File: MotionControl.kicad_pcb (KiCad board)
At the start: 2 copper layers, 180 x 80 mm, 176 parts, among them J1 Screw_Terminal_01x02, J10 Screw_Terminal_01x02, J11 Screw_Terminal_01x02, J2 Conn_ARM_JTAG_SWD_10, J3 Screw_Terminal_01x04, J5 Screw_Terminal_01x04, J6 Screw_Terminal_01x04, J7 Screw_Terminal_01x04, J8 Screw_Terminal_01x02, J9 Screw_Terminal_01x02, P1 USB_C_Plug_USB2.0, Q1 2N7002, Q10 Q_NMOS_DGS, Q11 Q_NMOS_DGS, Q12 Q_NMOS_DGS, Q13 Q_NMOS_DGS, Q14 Q_NMOS_DGS, Q15 Q_NMOS_DGS, Q16 Q_NMOS_DGS, Q17 Q_NMOS_DGS, Q18 Q_NMOS_DGS, Q19 Q_NMOS_DGS, Q2 Q_NMOS_DGS, Q20 Q_NMOS_DGS, Q21 Q_NMOS_DGS, Q22 Q_NMOS_DGS, Q23 Q_NMOS_DGS, Q24 Q_NMOS_DGS, Q25 Q_NMOS_DGS, Q26 Q_NMOS_DGS, Q27 Q_NMOS_DGS, Q28 Q_NMOS_DGS, Q29 Q_NMOS_DGS, Q3 Q_NMOS_DGS, Q30 Q_NMOS_DGS, Q31 Q_NMOS_DGS, Q32 Q_NMOS_DGS, Q33 Q_NMOS_DGS, Q4 Q_NMOS_DGS, Q5 Q_NMOS_DGS, Q6 Q_NMOS_DGS, Q7 Q_NMOS_DGS, Q8 Q_NMOS_DGS, Q9 Q_NMOS_DGS, SW1 SW_Push, U1 ATSAMD21J18A-A, U2 AP2112K-3.3, U3 TMC5160A-TA, U4 TMC5160A-TA, U5 TMC5160A-TA, U6 TMC5160A-TA, U7 TC4427, Y1 32.768kHz

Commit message: Route swd header
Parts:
- moved D6 27.1 mm to (130.0, 95.0), turned to 90 degrees
- moved J2 23.5 mm to (123.7, 86.1), turned to 90 degrees
- moved R9 20.7 mm to (130.0, 92.3), turned to 90 degrees
- moved D5 17.6 mm to (127.7, 95.0), turned to 90 degrees
- moved R8 11.4 mm to (127.7, 92.3), turned to 90 degrees
- moved C7 0.46 mm to (156.3, 81.7)
- moved C11 0.41 mm to (157.4, 81.7)
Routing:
- net /Steppers/MISO: track 0.00 -> 74.7 mm, vias 0 -> 2
- net /Steppers/MOSI: track 0.00 -> 71.1 mm, vias 0 -> 2
- net /Steppers/SCK: track 0.00 -> 67.1 mm, vias 0 -> 2
- net +5V: track 266.2 -> 326.4 mm, vias 1 -> 2
- net SWDCLK: track 0.00 -> 45.5 mm
- net PA27_TX_LED: track 0.00 -> 38.5 mm
- net SWDIO: track 0.00 -> 38.2 mm
- net /RESETn: track 16.0 -> 50.9 mm, vias 0 -> 2
- net +3V3: track 302.7 -> 331.1 mm, vias 0 -> 2
- net PB03_RX_LED: track 0.00 -> 28.1 mm, vias 0 -> 2
- net Net-(D6-A): track 0.00 -> 1.45 mm
- net Net-(D5-A): track 0.00 -> 1.45 mm
- net /Steppers/Stepper Unit/LED_OUT: track 49.5 -> 50.0 mm, vias 0 -> 2
- net GND: vias 74 -> 88
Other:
- board text added: "RX"
- board text added: "SWD"
- board text added: "TX"

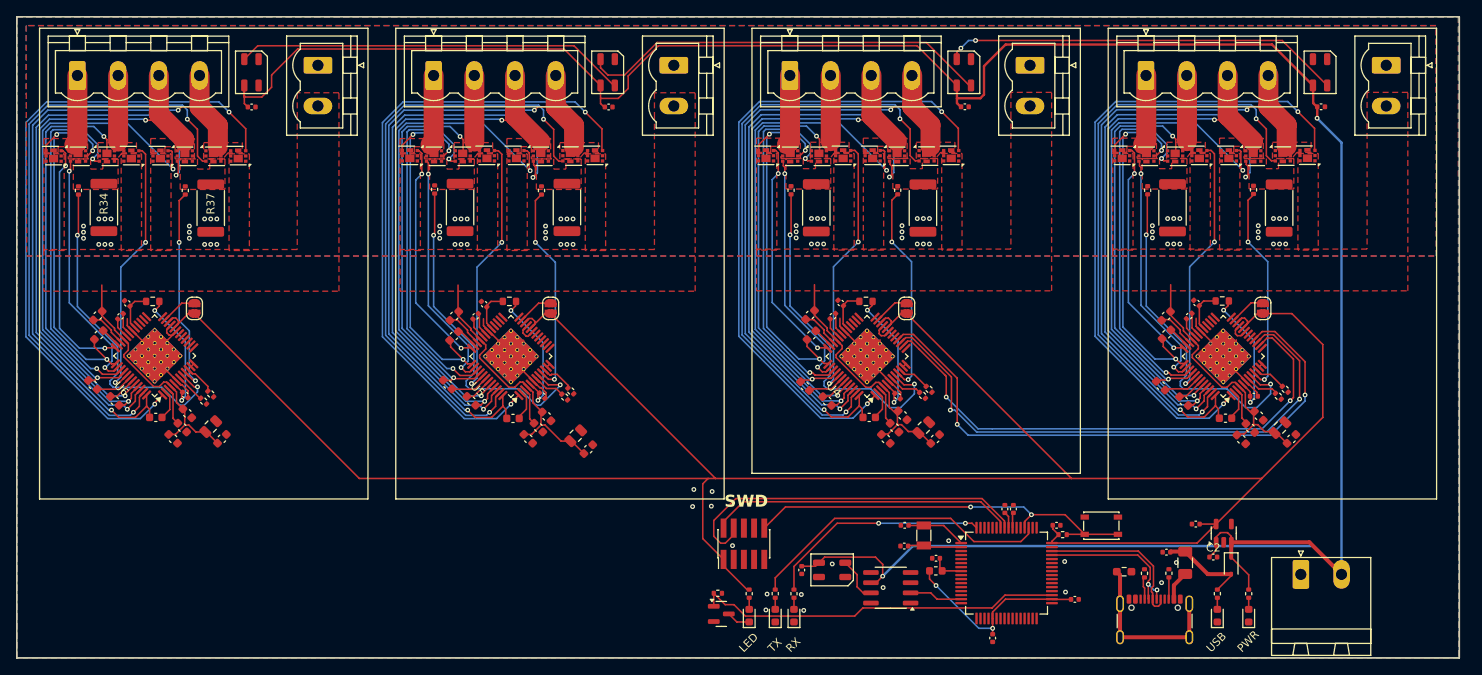
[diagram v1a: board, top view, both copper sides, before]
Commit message: Begin spi routing
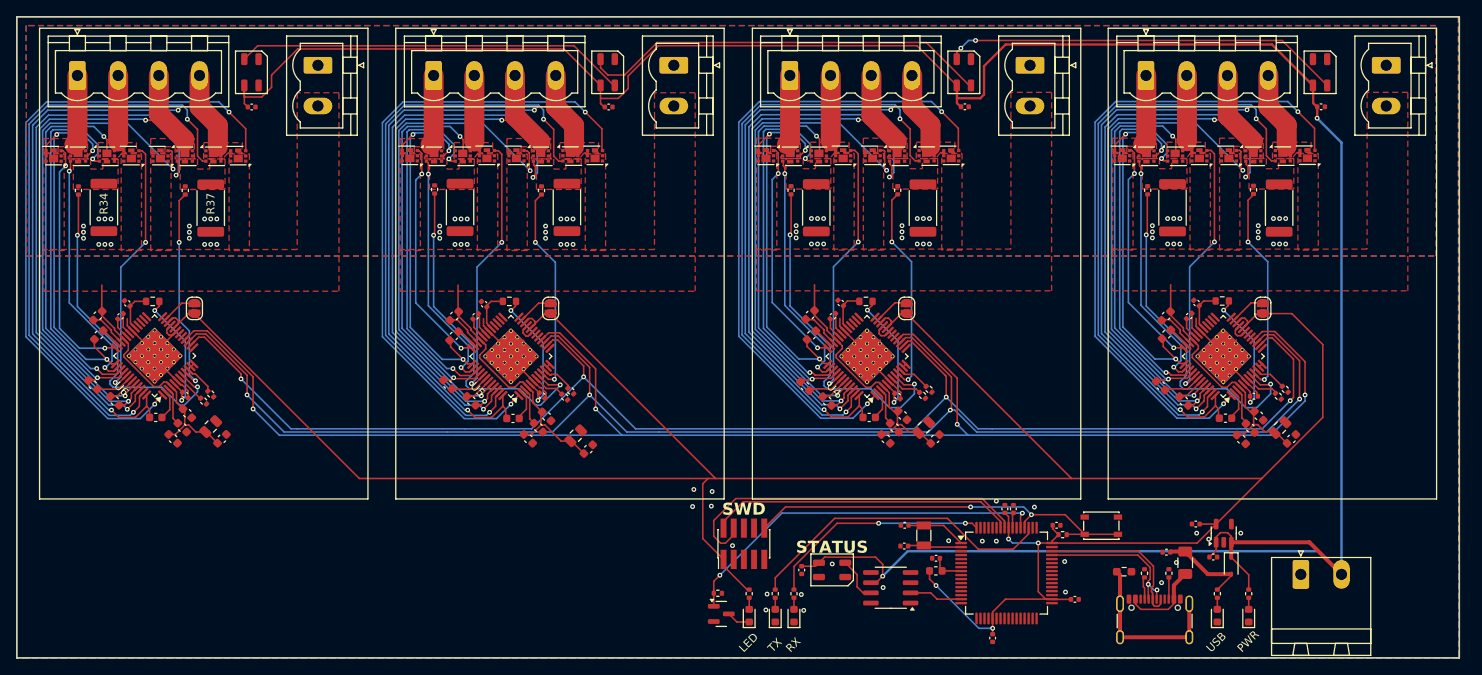
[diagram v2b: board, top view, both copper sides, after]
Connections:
- Q1 pad 1: PA16_LED -> PA28_LED
- R5 pad 2: PA16_LED -> PA28_LED
- U1 pad 35: PA16_LED -> unconnected-(U1-PA16-Pad35)
- U1 pad 53: unconnected-(U1-PA28-Pad53) -> PA28_LED
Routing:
- net /Steppers/MISO: track 74.7 -> 199.2 mm, vias 2 -> 4
- net /Steppers/MOSI: track 71.1 -> 189.2 mm, vias 2 -> 4
- net /Steppers/SCK: track 67.1 -> 181.4 mm, vias 2 -> 4
- net PA28_LED: track 0.00 -> 47.1 mm, vias 0 -> 2
- net PA16_LED: track 46.1 -> 0.00 mm
- net +3V3: track 331.1 -> 346.2 mm, vias 2 -> 4
- net Net-(F1-Pad1): track 3.73 -> 10.3 mm
- net PA27_TX_LED: track 38.5 -> 39.3 mm
- net +5V: track 326.4 -> 325.9 mm
- net GND: vias 88 -> 95
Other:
- board text added: "STATUS"

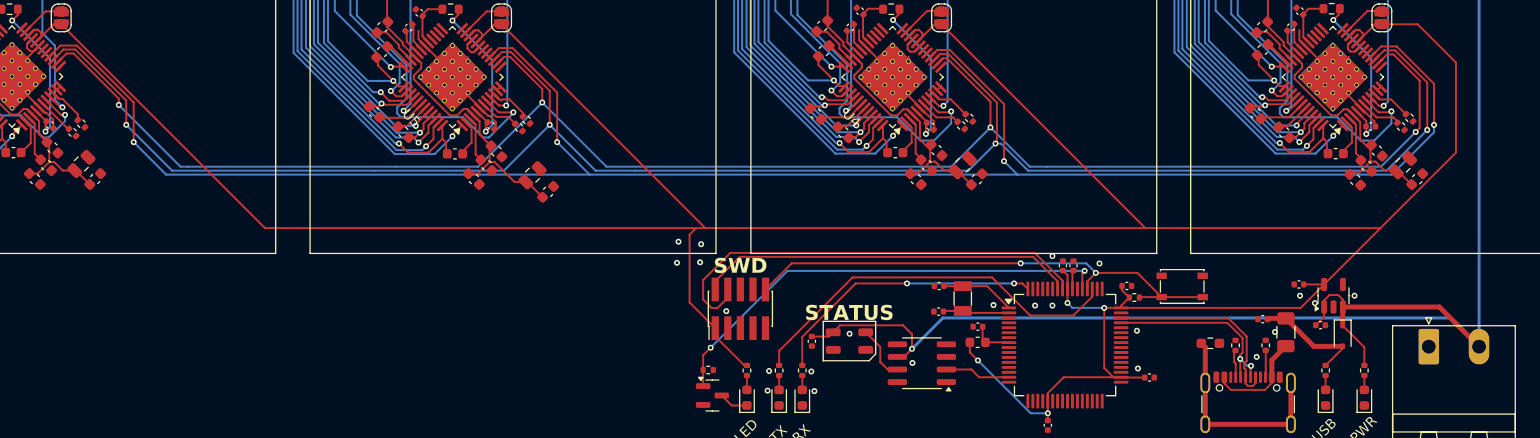
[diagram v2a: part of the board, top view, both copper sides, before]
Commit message: Route tmc spi busses, cs
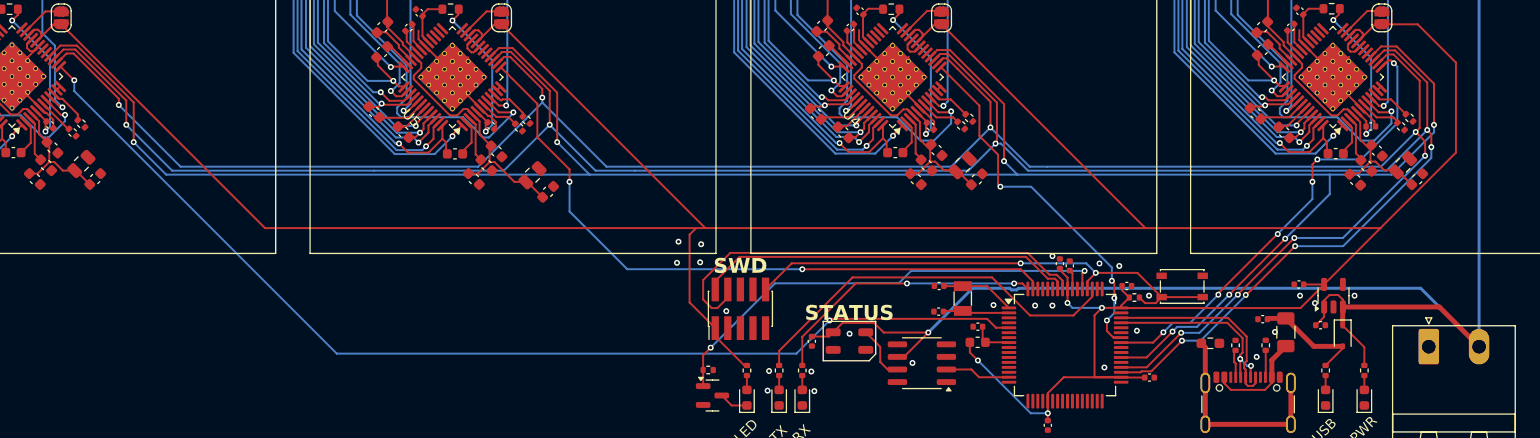
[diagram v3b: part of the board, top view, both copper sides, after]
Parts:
- moved C7 0.38 mm to (156.0, 81.5)
- moved C11 0.38 mm to (157.0, 81.7)
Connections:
- U1 pad 35: unconnected-(U1-PA16-Pad35) -> PA16_TMC_MOSI
- U1 pad 36: unconnected-(U1-PA17-Pad36) -> PA17_TMC_SCK
- U1 pad 38: unconnected-(U1-PA19-Pad38) -> PA19_TMC_MISO
- U1 pad 41: unconnected-(U1-PA20-Pad41) -> PA20_TMC_CSn1
- U1 pad 42: unconnected-(U1-PA21-Pad42) -> PA21_TMC_CSn2
- U1 pad 5: unconnected-(U1-PB04-Pad5) -> PB04_TMC_CSn4
- U1 pad 63: unconnected-(U1-PB02-Pad63) -> PB02_TMC_CSn3
- U3 pad 13: /Steppers/CSn1 -> PA20_TMC_CSn1
- U3 pad 14: /Steppers/SCK -> PA17_TMC_SCK
- U3 pad 15: /Steppers/MOSI -> PA16_TMC_MOSI
- U3 pad 16: /Steppers/MISO -> PA19_TMC_MISO
- U4 pad 13: /Steppers/CSn2 -> PA21_TMC_CSn2
- U4 pad 14: /Steppers/SCK -> PA17_TMC_SCK
- U4 pad 15: /Steppers/MOSI -> PA16_TMC_MOSI
- U4 pad 16: /Steppers/MISO -> PA19_TMC_MISO
- U5 pad 13: /Steppers/CSn3 -> PB02_TMC_CSn3
- U5 pad 14: /Steppers/SCK -> PA17_TMC_SCK
- U5 pad 15: /Steppers/MOSI -> PA16_TMC_MOSI
- U5 pad 16: /Steppers/MISO -> PA19_TMC_MISO
- U6 pad 13: /Steppers/CSn4 -> PB04_TMC_CSn4
- U6 pad 14: /Steppers/SCK -> PA17_TMC_SCK
- U6 pad 15: /Steppers/MOSI -> PA16_TMC_MOSI
- U6 pad 16: /Steppers/MISO -> PA19_TMC_MISO
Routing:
- net PA16_TMC_MOSI: track 0.00 -> 232.5 mm, vias 0 -> 8
- net PA19_TMC_MISO: track 0.00 -> 229.1 mm, vias 0 -> 7
- net PA17_TMC_SCK: track 0.00 -> 223.7 mm, vias 0 -> 8
- net /Steppers/MISO: track 199.2 -> 0.00 mm, vias 4 -> 0
- net /Steppers/MOSI: track 189.2 -> 0.00 mm, vias 4 -> 0
- net /Steppers/SCK: track 181.4 -> 0.00 mm, vias 4 -> 0
- net PB04_TMC_CSn4: track 0.00 -> 110.2 mm, vias 0 -> 2
- net PB02_TMC_CSn3: track 0.00 -> 67.9 mm, vias 0 -> 2
- net PA20_TMC_CSn1: track 0.00 -> 47.1 mm, vias 0 -> 6
- net PA21_TMC_CSn2: track 0.00 -> 37.7 mm, vias 0 -> 4
- net +5V: track 325.9 -> 328.8 mm
- net +3V3: track 346.2 -> 348.4 mm
- net GND: vias 95 -> 97

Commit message: Begin addition of mag sensor conns
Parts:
- added J12: Conn_01x07_MountingPin, Connector_JST:JST_SH_BM07B-SRSS-TB_1x07-1MP_P1.00mm_Vertical, F.Cu at (57.3, 91.6)
- added J13: Conn_01x07_MountingPin, Connector_JST:JST_SH_BM07B-SRSS-TB_1x07-1MP_P1.00mm_Vertical, F.Cu at (43.1, 85.0)
- added J14: Conn_01x07_MountingPin, Connector_JST:JST_SH_BM07B-SRSS-TB_1x07-1MP_P1.00mm_Vertical, F.Cu at (43.1, 91.6)
- added J4: Conn_01x07_MountingPin, Connector_JST:JST_SH_BM07B-SRSS-TB_1x07-1MP_P1.00mm_Vertical, F.Cu at (57.3, 85.0)
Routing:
- net GND: track 50.7 -> 100.3 mm
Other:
- board text added: "1"
- board text added: "2"
- board text added: "3"
- board text added: "4"

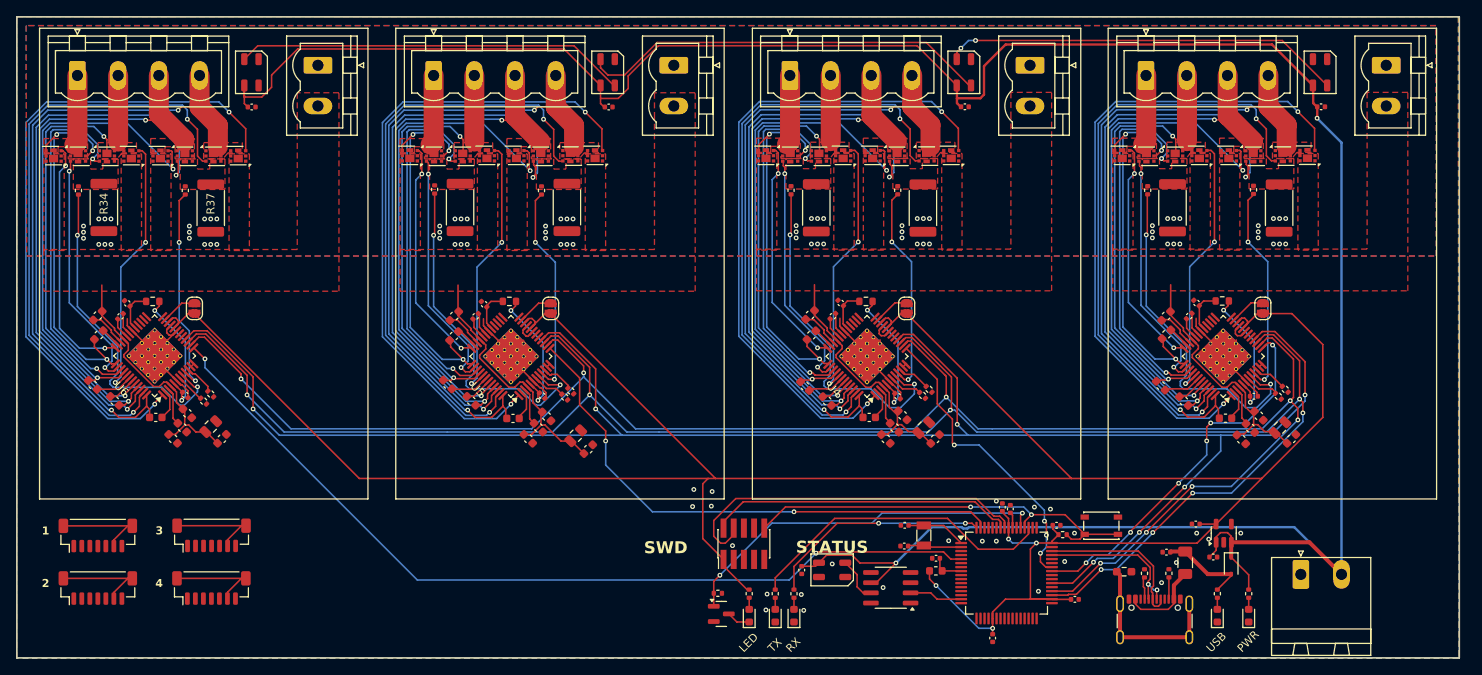
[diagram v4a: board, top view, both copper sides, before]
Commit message: silkscreen changes, start routing spi
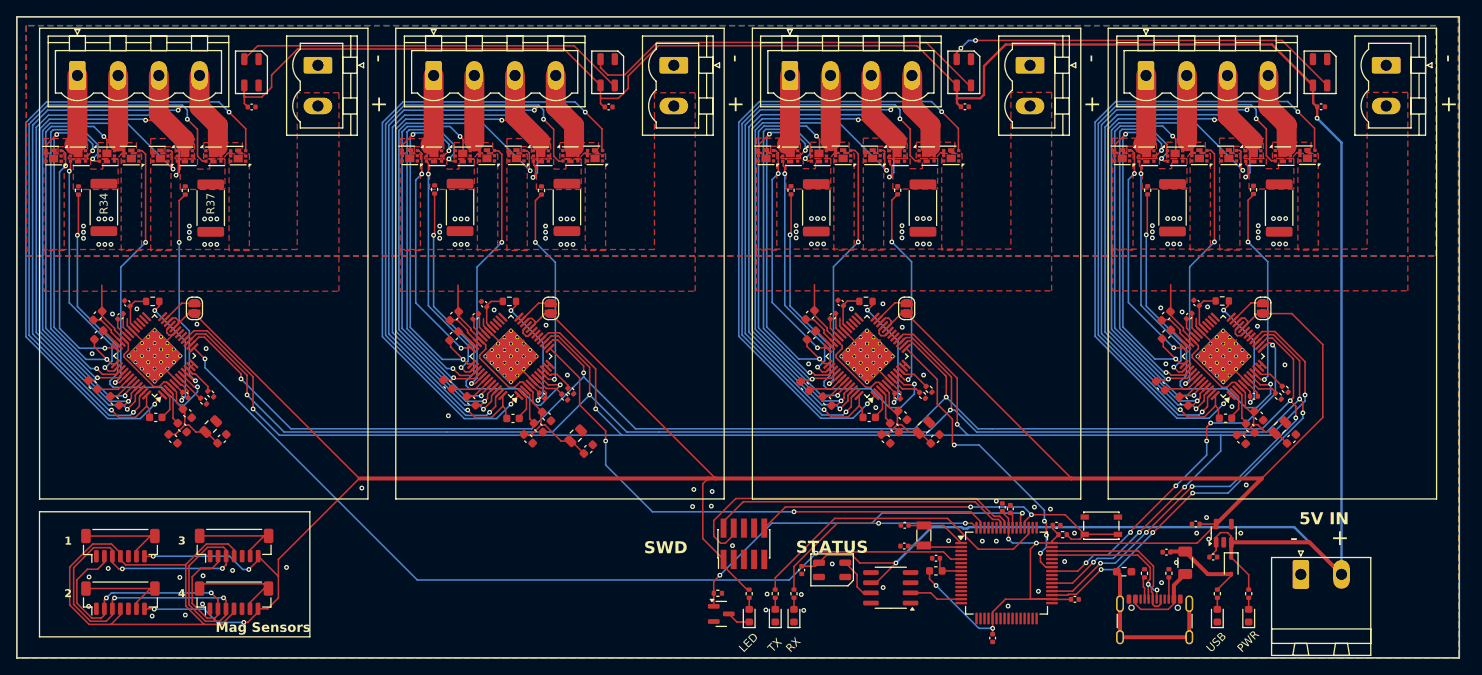
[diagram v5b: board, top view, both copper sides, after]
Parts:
- moved J13 3.09 mm to (45.9, 86.3)
- moved J4 3.09 mm to (60.1, 86.3)
- moved J12 3.09 mm to (60.1, 92.9)
- moved J14 3.09 mm to (45.9, 92.9)
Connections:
- J12 pad 3: /Mag Sensors/MOSI -> /Mag Sensors/MISO
- J14 pad 3: /Mag Sensors/MOSI -> /Mag Sensors/MISO
- J4 pad 3: /Mag Sensors/MOSI -> /Mag Sensors/MISO
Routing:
- net /Mag Sensors/MISO: track 0.00 -> 69.2 mm, vias 0 -> 4
- net /Mag Sensors/CLK: track 0.00 -> 63.6 mm
- net +3V3: track 348.4 -> 405.9 mm, vias 4 -> 8
- net /Mag Sensors/MOSI: track 0.00 -> 43.3 mm, vias 0 -> 2
- net GND: track 100.3 -> 100.8 mm, vias 97 -> 133
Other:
- board text added: "+"
- board text added: "-"
- board text added: "5V IN"
- board text added: "Mag Sensors"
